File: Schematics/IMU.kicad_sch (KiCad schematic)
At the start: 4 parts, among them U5 LSM6DS3TR-C

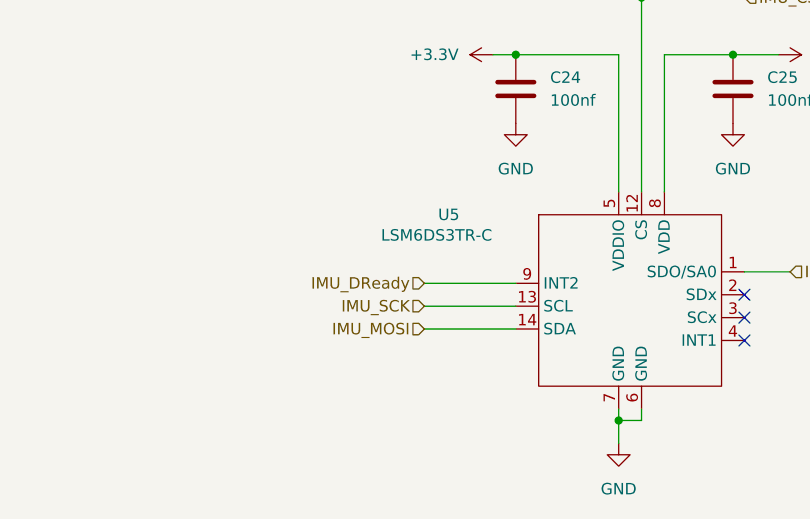
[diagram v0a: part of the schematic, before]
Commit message: started new design with esp32
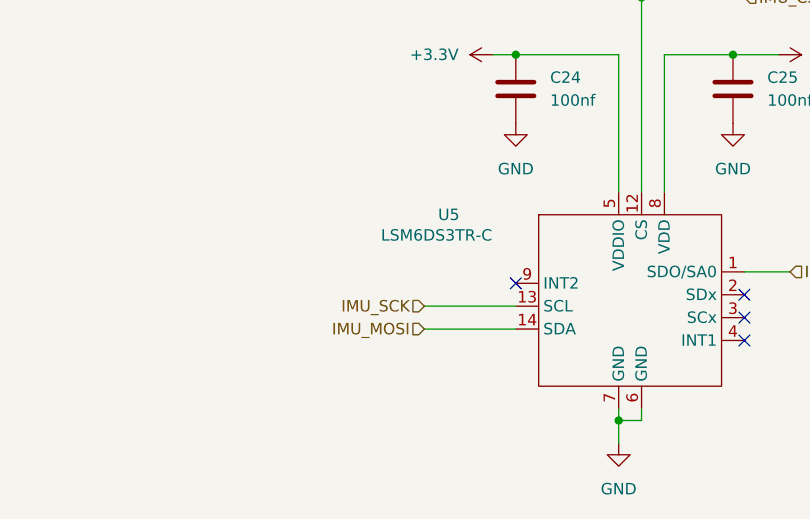
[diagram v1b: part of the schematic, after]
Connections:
- net IMU_DReady: no longer names the net of U5.9 (INT2)
- no-connect marks 3 -> 4
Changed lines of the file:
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@@
 		(at 151.13 111.76)
+	)
+	(no_connect
+		(at 125.73 107.95)
 	)
 	(wire
@@
 		(pts
 			(xy 139.7 123.19) (xy 137.16 123.19)
-		)
-		(stroke
-			(width 0)
-			(type default)
-		)
-	)
-	(wire
-		(pts
-			(xy 115.57 107.95) (xy 125.73 107.95)
 		)
 		(stroke
@@
 		)
 	)
-	(hierarchical_label "IMU_DReady"
-		(shape input)
-		(at 115.57 107.95 180)
-		(effects
-			(font
-				(size 1.27 1.27)
-			)
-			(justify right)
-		)
-	)

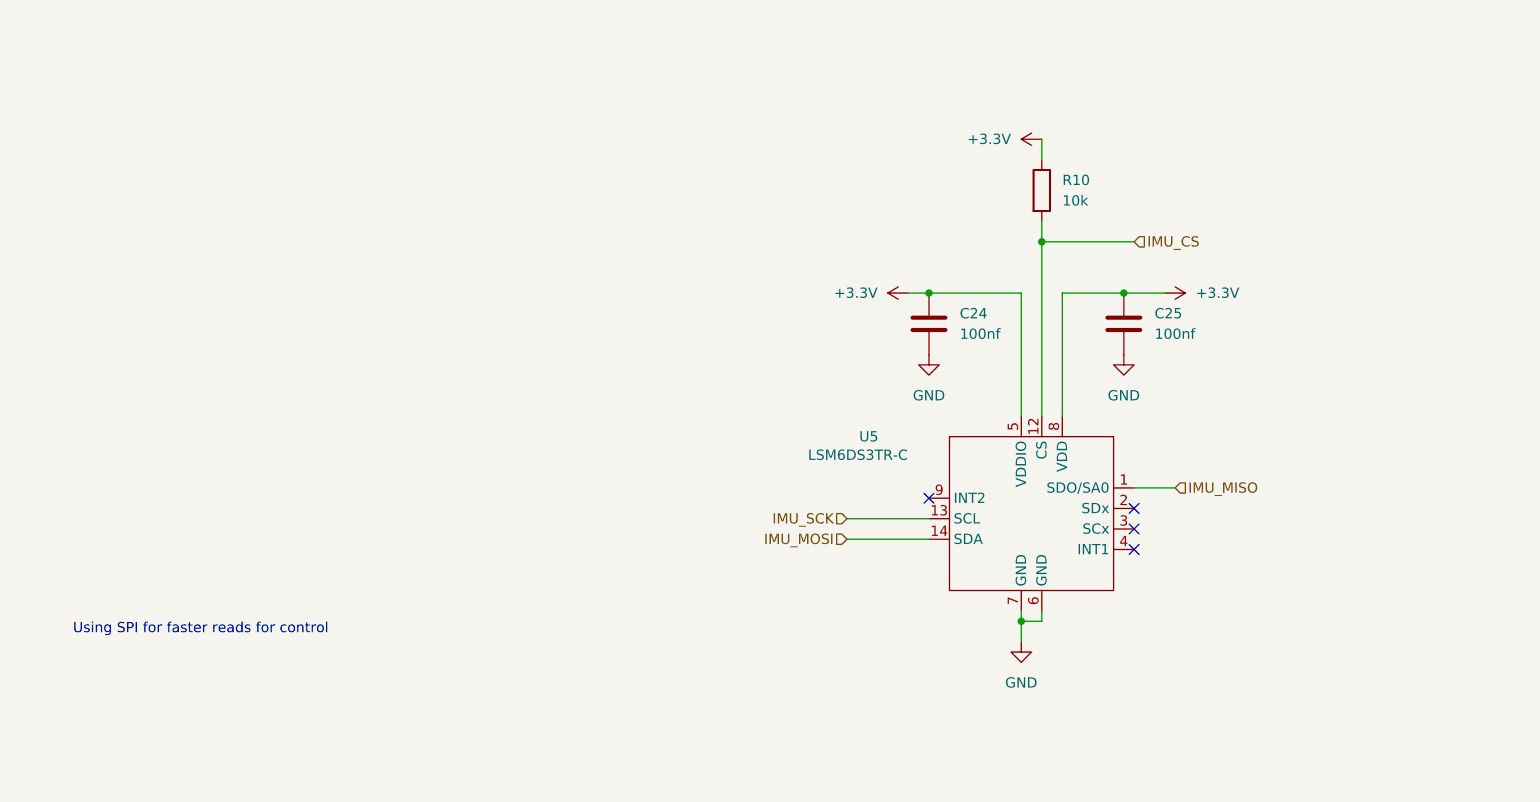
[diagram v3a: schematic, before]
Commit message: Added encoder connection for parafoil motor position information, in buy order ready for purchase
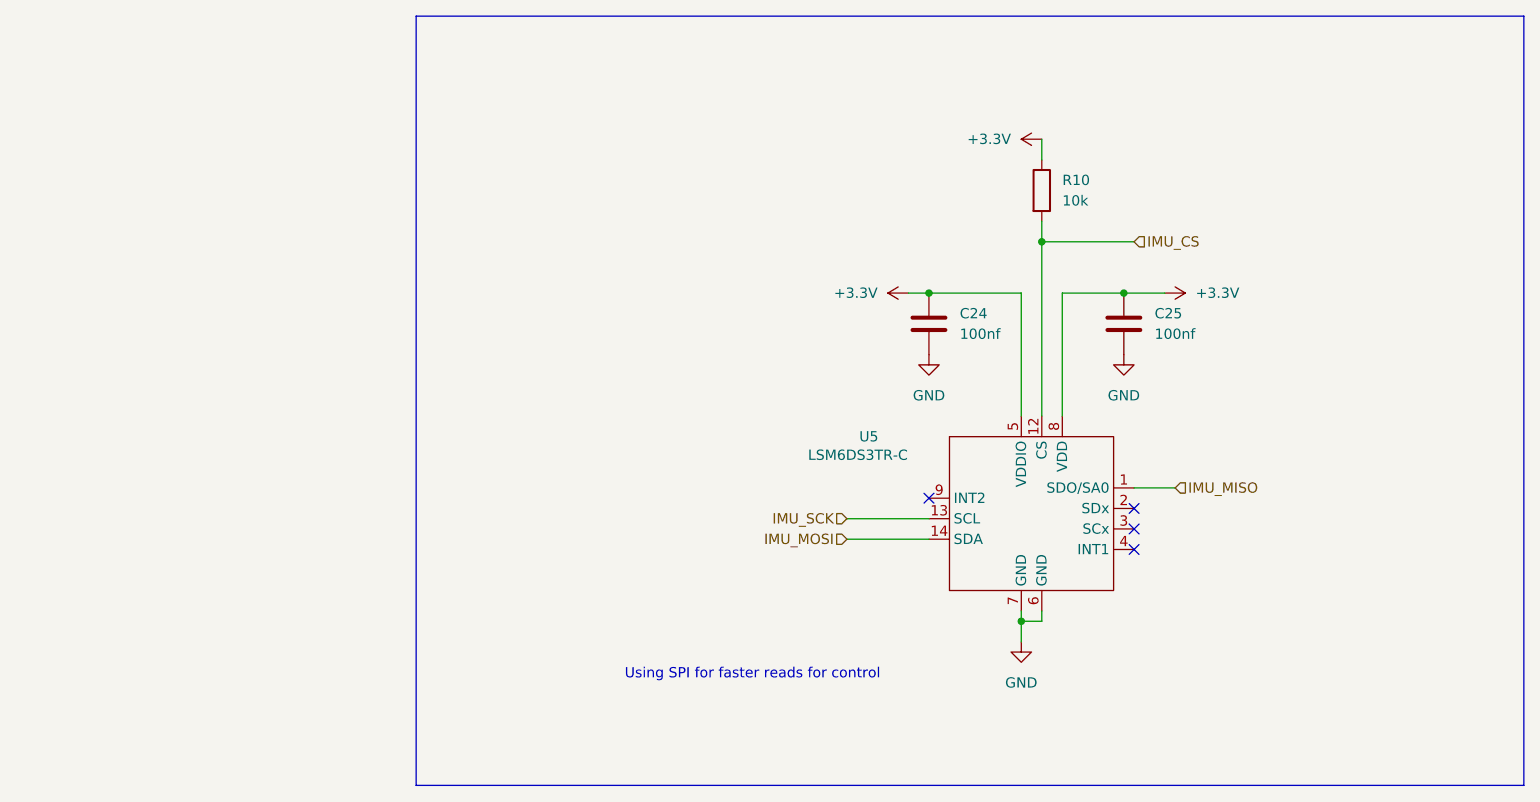
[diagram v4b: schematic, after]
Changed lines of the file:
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@@
 	(generator_version "10.0")
 	(paper "A4")
+	(rectangle
+		(start 62.23 48.26)
+		(end 199.39 143.51)
+		(stroke
+			(width 0)
+			(type default)
+		)
+		(fill
+			(type none)
+		)
+	)
 	(text "Using SPI for faster reads for control"
 		(exclude_from_sim no)
-		(at 35.56 124.206 0)
+		(at 103.886 129.794 0)
 		(effects
 			(font
